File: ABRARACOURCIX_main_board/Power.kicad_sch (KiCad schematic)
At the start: 37 parts, among them J10 XT60PW-M, J11 Conn_01x02_Pin, J12 Conn_01x02_Pin, J8 XT60PW-M, J9 XT60PW-F, Q2 DSS20200L-7-PNP, Q3 IKD15N60R, Q4 NPN-DSS20201L-7, Q5 NTR4101PT1G, U3 Current_sens_ACS712ELCTR-20A-T, U4 AZ1117CH-3.3TRG1, U5 LMC6482AIMX/NOPB, U6 LMC6482AIMX/NOPB

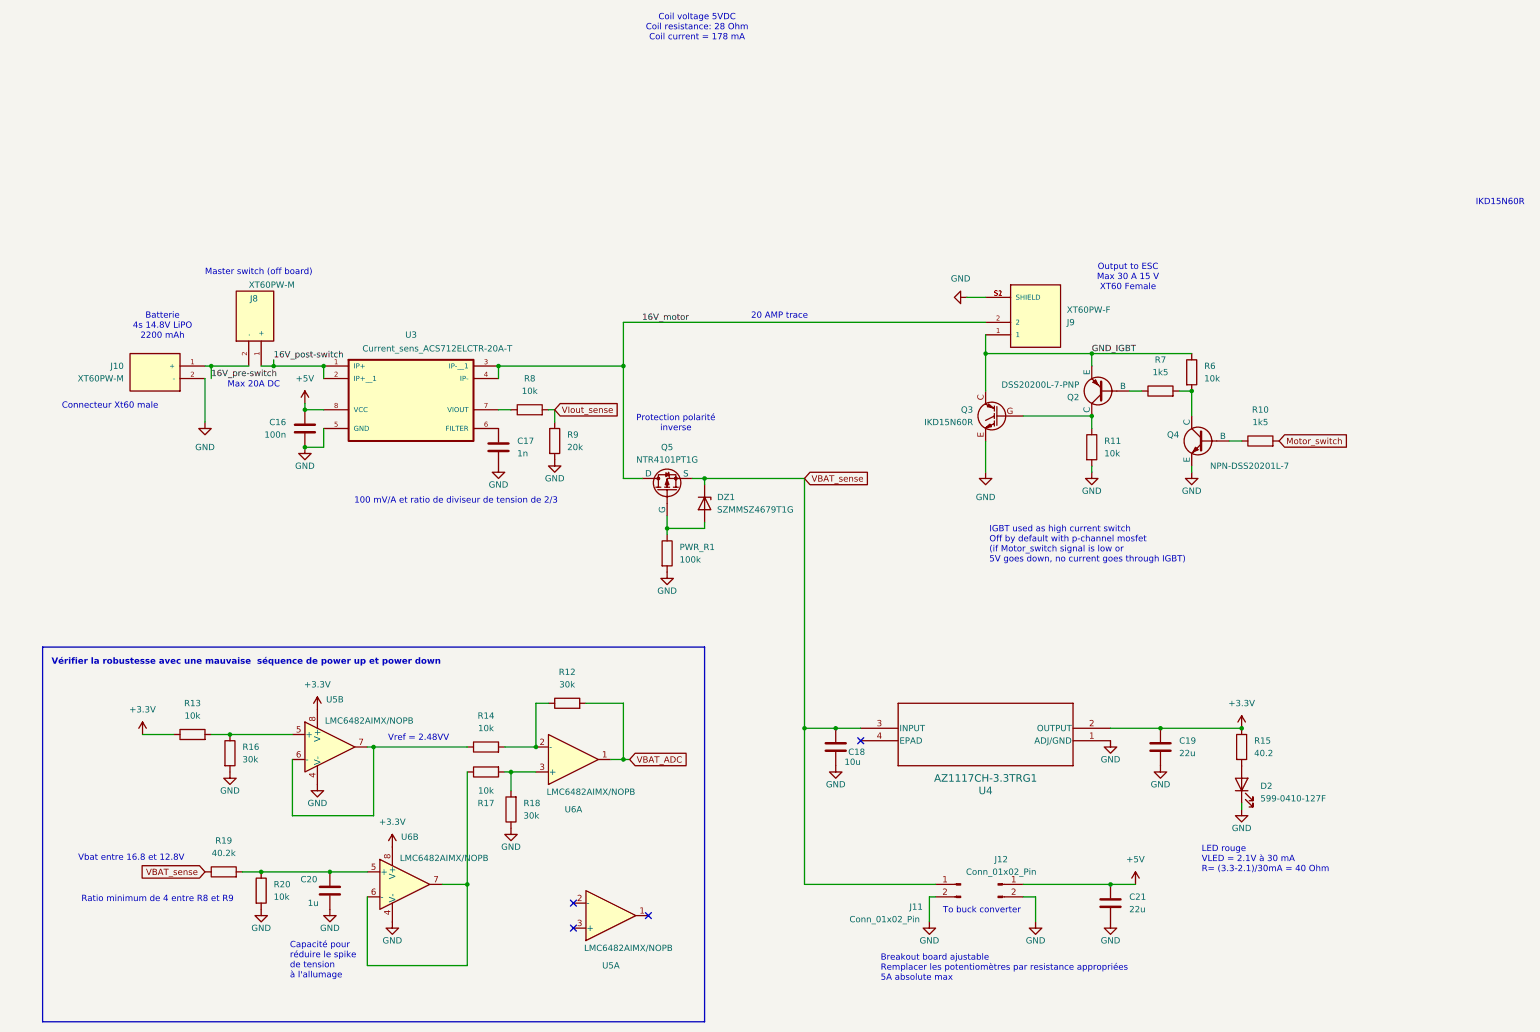
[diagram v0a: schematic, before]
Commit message: micro_USB
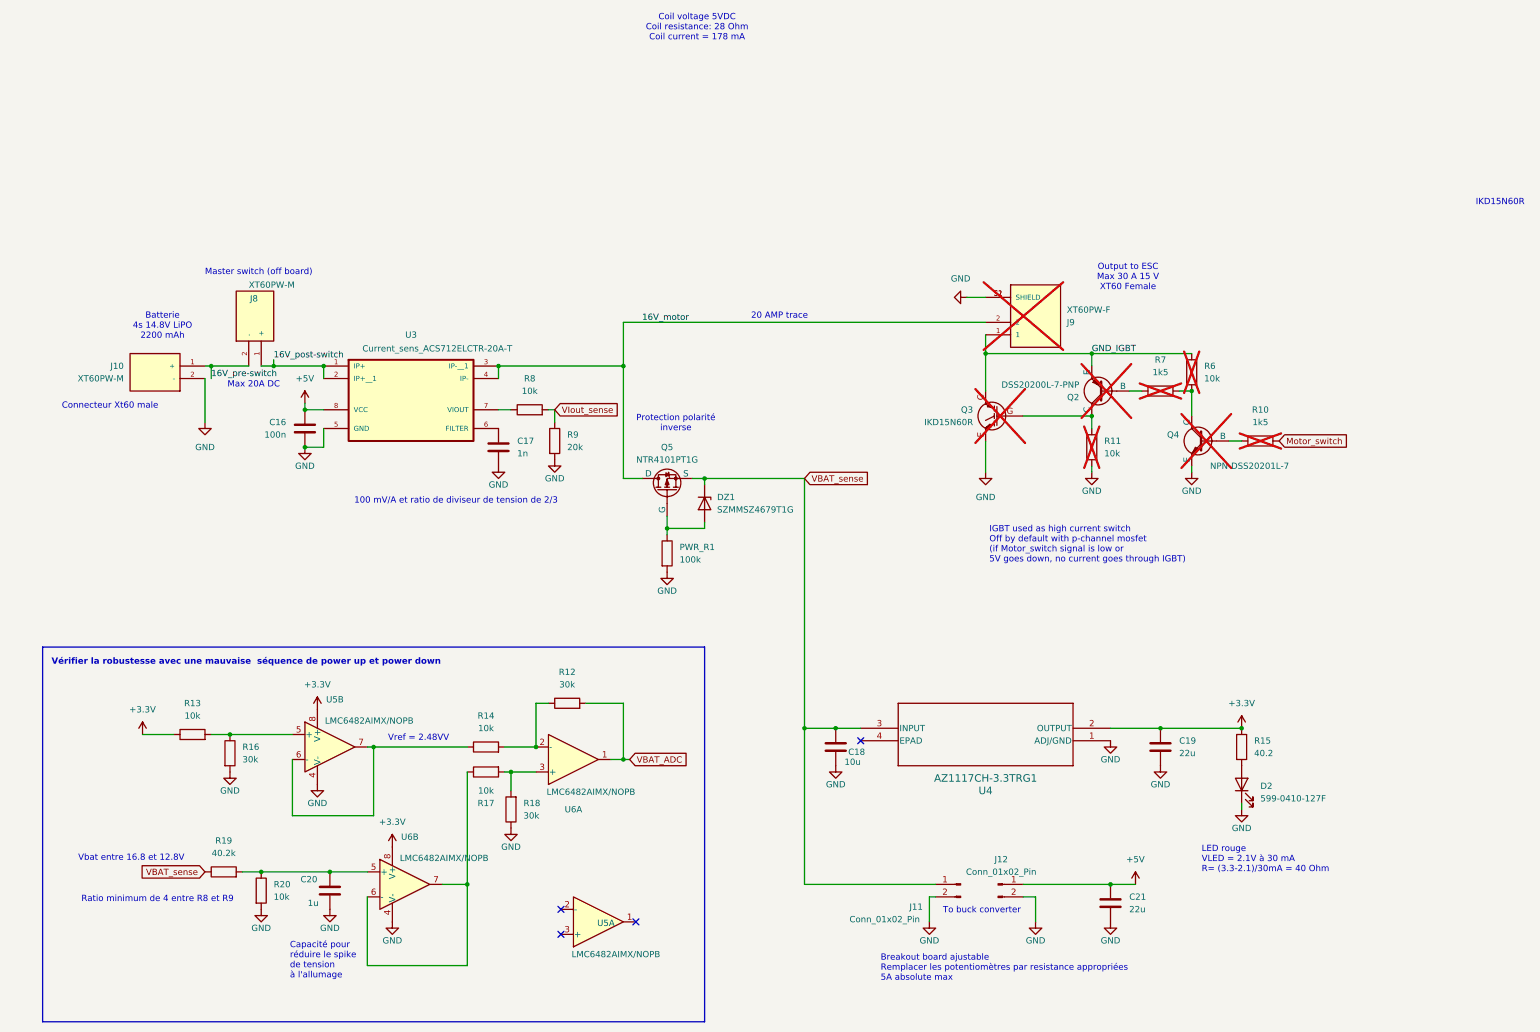
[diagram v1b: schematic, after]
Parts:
- J9: now not fitted
- Q2, Q3, Q4, R10, R11, R6, R7: now not fitted; now left out of the parts list
